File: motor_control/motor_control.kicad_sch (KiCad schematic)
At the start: 24 parts, among them J1 GPIO, J2 MotA, J3 MotB, J4 MOT_POW, J5 UART, J6 SPI, J7 I2C, J8 VBUS_OUT, SW1 PU, SW2 PD, U1 HC-SR04

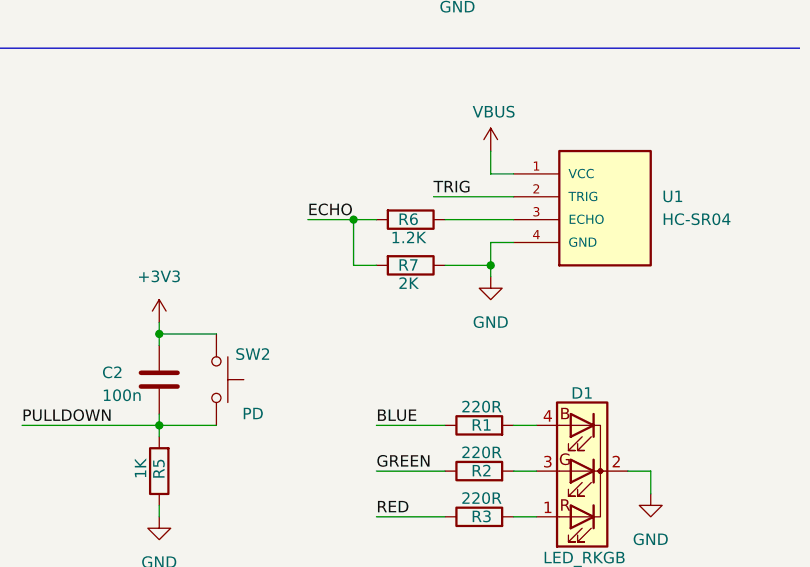
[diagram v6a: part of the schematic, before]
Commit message: fix hcsr04 voltage divider
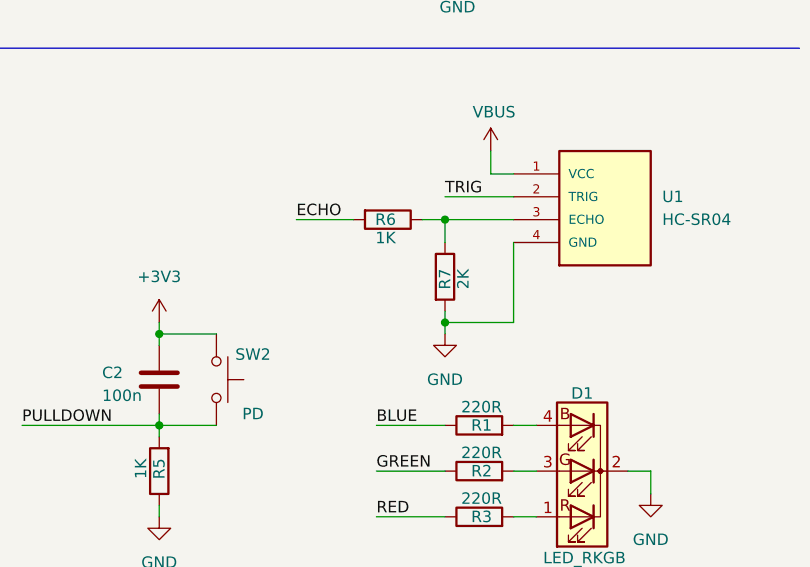
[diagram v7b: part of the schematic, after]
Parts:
- R6: value 1.2K -> 1K
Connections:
- net ECHO: no longer R7.2
- net GND: now also R7.2; no longer R7.1
- net at R6.1, U1.3 (ECHO): now also R7.1
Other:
- moved on the sheet: R6, R7
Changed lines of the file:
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@@
 	)
 	(junction
+		(at 227.33 125.73)
+		(diameter 0)
+		(color 0 0 0 0)
+	)
+	(junction
 		(at 195.58 138.43)
 		(diameter 0)
@@
 	)
 	(junction
-		(at 217.17 125.73)
-		(diameter 0)
-		(color 0 0 0 0)
-	)
-	(junction
 		(at 165.1 158.75)
 		(diameter 0)
@@
 	)
 	(junction
-		(at 232.41 130.81)
-		(diameter 0)
-		(color 0 0 0 0)
-	)
-	(junction
 		(at 165.1 148.59)
 		(diameter 0)
@@
 	)
 	(junction
+		(at 227.33 137.16)
+		(diameter 0)
+		(color 0 0 0 0)
+	)
+	(junction
 		(at 55.88 27.94)
 		(diameter 1.016)
@@
 	(wire
 		(pts
-			(xy 232.41 128.27) (xy 232.41 130.81)
-		)
-		(stroke
-			(width 0)
-			(type default)
-		)
-	)
-	(wire
-		(pts
 			(xy 49.53 166.37) (xy 59.69 166.37)
 		)
@@
 	(wire
 		(pts
+			(xy 227.33 137.16) (xy 227.33 138.43)
+		)
+		(stroke
+			(width 0)
+			(type default)
+		)
+	)
+	(wire
+		(pts
 			(xy 58.42 38.1) (xy 58.42 58.42)
 		)
@@
 	(wire
 		(pts
+			(xy 224.79 125.73) (xy 227.33 125.73)
+		)
+		(stroke
+			(width 0)
+			(type default)
+		)
+	)
+	(wire
+		(pts
 			(xy 185.42 67.31) (xy 205.74 67.31)
 		)
@@
 	(wire
 		(pts
+			(xy 227.33 125.73) (xy 227.33 128.27)
+		)
+		(stroke
+			(width 0)
+			(type default)
+		)
+	)
+	(wire
+		(pts
 			(xy 85.09 168.91) (xy 93.98 168.91)
 		)
@@
 	(wire
 		(pts
-			(xy 232.41 130.81) (xy 232.41 132.08)
-		)
-		(stroke
-			(width 0)
-			(type default)
-		)
-	)
-	(wire
-		(pts
 			(xy 260.35 22.86) (xy 260.35 25.4)
 		)
@@
 	(wire
 		(pts
+			(xy 210.82 125.73) (xy 217.17 125.73)
+		)
+		(stroke
+			(width 0)
+			(type default)
+		)
+	)
+	(wire
+		(pts
 			(xy 251.46 57.15) (xy 264.16 57.15)
 		)
@@
 	(wire
 		(pts
-			(xy 165.1 147.32) (xy 165.1 148.59)
+			(xy 227.33 137.16) (xy 234.95 137.16)
 		)
 		(stroke
@@
 	(wire
 		(pts
-			(xy 40.64 181.61) (xy 59.69 181.61)
+			(xy 165.1 147.32) (xy 165.1 148.59)
 		)
 		(stroke
@@
 	(wire
 		(pts
-			(xy 165.1 148.59) (xy 165.1 149.86)
+			(xy 40.64 181.61) (xy 59.69 181.61)
 		)
 		(stroke
@@
 	(wire
 		(pts
-			(xy 76.2 68.58) (xy 73.66 68.58)
+			(xy 165.1 148.59) (xy 165.1 149.86)
 		)
 		(stroke
 			(width 0)
-			(type solid)
+			(type default)
 		)
 	)
 	(wire
 		(pts
-			(xy 226.06 123.19) (xy 234.95 123.19)
+			(xy 76.2 68.58) (xy 73.66 68.58)
 		)
 		(stroke
 			(width 0)
-			(type default)
+			(type solid)
 		)
 	)
@@
 	(wire
 		(pts
-			(xy 217.17 130.81) (xy 217.17 125.73)
-		)
-		(stroke
-			(width 0)
-			(type default)
-		)
-	)
-	(wire
-		(pts
 			(xy 76.2 43.18) (xy 76.2 50.8)
 		)
@@
 	(wire
 		(pts
-			(xy 234.95 128.27) (xy 232.41 128.27)
-		)
-		(stroke
-			(width 0)
-			(type default)
-		)
-	)
-	(wire
-		(pts
 			(xy 76.2 43.18) (xy 73.66 43.18)
 		)
@@
 	(wire
 		(pts
-			(xy 165.1 158.75) (xy 171.45 158.75)
+			(xy 227.33 135.89) (xy 227.33 137.16)
 		)
 		(stroke
@@
 	(wire
 		(pts
-			(xy 73.66 48.26) (xy 100.33 48.26)
+			(xy 165.1 158.75) (xy 171.45 158.75)
 		)
 		(stroke
 			(width 0)
-			(type solid)
+			(type default)
 		)
 	)
 	(wire
 		(pts
-			(xy 73.66 38.1) (xy 100.33 38.1)
+			(xy 73.66 48.26) (xy 100.33 48.26)
 		)
 		(stroke
@@
 	(wire
 		(pts
-			(xy 227.33 125.73) (xy 234.95 125.73)
+			(xy 73.66 38.1) (xy 100.33 38.1)
 		)
 		(stroke
 			(width 0)
-			(type default)
+			(type solid)
 		)
 	)
@@
 	(wire
 		(pts
-			(xy 227.33 130.81) (xy 232.41 130.81)
-		)
-		(stroke
-			(width 0)
-			(type default)
-		)
-	)
-	(wire
-		(pts
 			(xy 76.2 30.48) (xy 73.66 30.48)
 		)
@@
 	(wire
 		(pts
-			(xy 201.93 138.43) (xy 195.58 138.43)
+			(xy 227.33 123.19) (xy 234.95 123.19)
 		)
 		(stroke
@@
 	(wire
 		(pts
-			(xy 217.17 125.73) (xy 219.71 125.73)
+			(xy 201.93 138.43) (xy 195.58 138.43)
 		)
 		(stroke
@@
 	(wire
 		(pts
+			(xy 227.33 125.73) (xy 234.95 125.73)
+		)
+		(stroke
+			(width 0)
+			(type default)
+		)
+	)
+	(wire
+		(pts
 			(xy 40.64 179.07) (xy 40.64 181.61)
 		)
@@
 	(wire
 		(pts
-			(xy 219.71 130.81) (xy 217.17 130.81)
+			(xy 234.95 128.27) (xy 234.95 137.16)
 		)
 		(stroke
@@
 	(wire
 		(pts
-			(xy 212.09 125.73) (xy 217.17 125.73)
-		)
-		(stroke
-			(width 0)
-			(type default)
-		)
-	)
-	(wire
-		(pts
 			(xy 31.75 129.54) (xy 43.18 129.54)
 		)
@@
 	)
 	(label "ECHO"
-		(at 212.09 125.73 0)
+		(at 210.82 125.73 0)
 		(effects
 			(font
@@
 	)
 	(label "TRIG"
-		(at 226.06 123.19 0)
+		(at 227.33 123.19 0)
 		(effects
 			(font
@@
 	(symbol
 		(lib_id "Device:R")
-		(at 223.52 125.73 270)
+		(at 220.98 125.73 270)
 		(unit 1)
 		(exclude_from_sim no)
@@
 		(dnp no)
 		(property "Reference" "R6"
-			(at 223.266 125.73 90)
+			(at 220.726 125.73 90)
 			(effects
 				(font
@@
 			)
 		)
-		(property "Value" "1.2K"
-			(at 223.266 127.762 90)
+		(property "Value" "1K"
+			(at 220.726 127.762 90)
 			(effects
 				(font
@@
 		)
 		(property "Footprint" "Resistor_THT:R_Axial_DIN0207_L6.3mm_D2.5mm_P7.62mm_Horizontal"
-			(at 223.52 123.952 90)
+			(at 220.98 123.952 90)
 			(effects
 				(font
@@
 		)
 		(property "Datasheet" "~"
-			(at 223.52 125.73 0)
+			(at 220.98 125.73 0)
 			(effects
 				(font
@@
 		)
 		(property "Description" "Resistor"
-			(at 223.52 125.73 0)
+			(at 220.98 125.73 0)
 			(effects
 				(font
@@
 	(symbol
 		(lib_id "Device:R")
-		(at 223.52 130.81 270)
+		(at 227.33 132.08 0)
 		(unit 1)
 		(exclude_from_sim no)
@@
 		(dnp no)
 		(property "Reference" "R7"
-			(at 223.266 130.81 90)
+			(at 227.33 132.334 90)
 			(effects
 				(font
@@
 		)
 		(property "Value" "2K"
-			(at 223.266 132.842 90)
+			(at 229.362 132.334 90)
 			(effects
 				(font
@@
 		)
 		(property "Footprint" "Resistor_THT:R_Axial_DIN0207_L6.3mm_D2.5mm_P7.62mm_Horizontal"
-			(at 223.52 129.032 90)
+			(at 225.552 132.08 90)
 			(effects
 				(font
@@
 		)
 		(property "Datasheet" "~"
-			(at 223.52 130.81 0)
+			(at 227.33 132.08 0)
 			(effects
 				(font
@@
 		)
 		(property "Description" "Resistor"
-			(at 223.52 130.81 0)
+			(at 227.33 132.08 0)
 			(effects
 				(font
@@
 	(symbol
 		(lib_id "power:GND")
-		(at 232.41 132.08 0)
+		(at 227.33 138.43 0)
 		(unit 1)
 		(exclude_from_sim no)
@@
 		(fields_autoplaced yes)
 		(property "Reference" "#PWR012"
-			(at 232.41 138.43 0)
+			(at 227.33 144.78 0)
 			(effects
 				(font
@@
 		)
 		(property "Value" "GND"
-			(at 232.41 137.16 0)
+			(at 227.33 143.51 0)
 			(effects
 				(font
@@
 		)
 		(property "Footprint" ""
-			(at 232.41 132.08 0)
+			(at 227.33 138.43 0)
 			(effects
 				(font
@@
 		)
 		(property "Datasheet" ""
-			(at 232.41 132.08 0)
+			(at 227.33 138.43 0)
 			(effects
 				(font
@@
 		)
 		(property "Description" "Power symbol creates a global label with name \"GND\" , ground"
-			(at 232.41 132.08 0)
+			(at 227.33 138.43 0)
 			(effects
 				(font

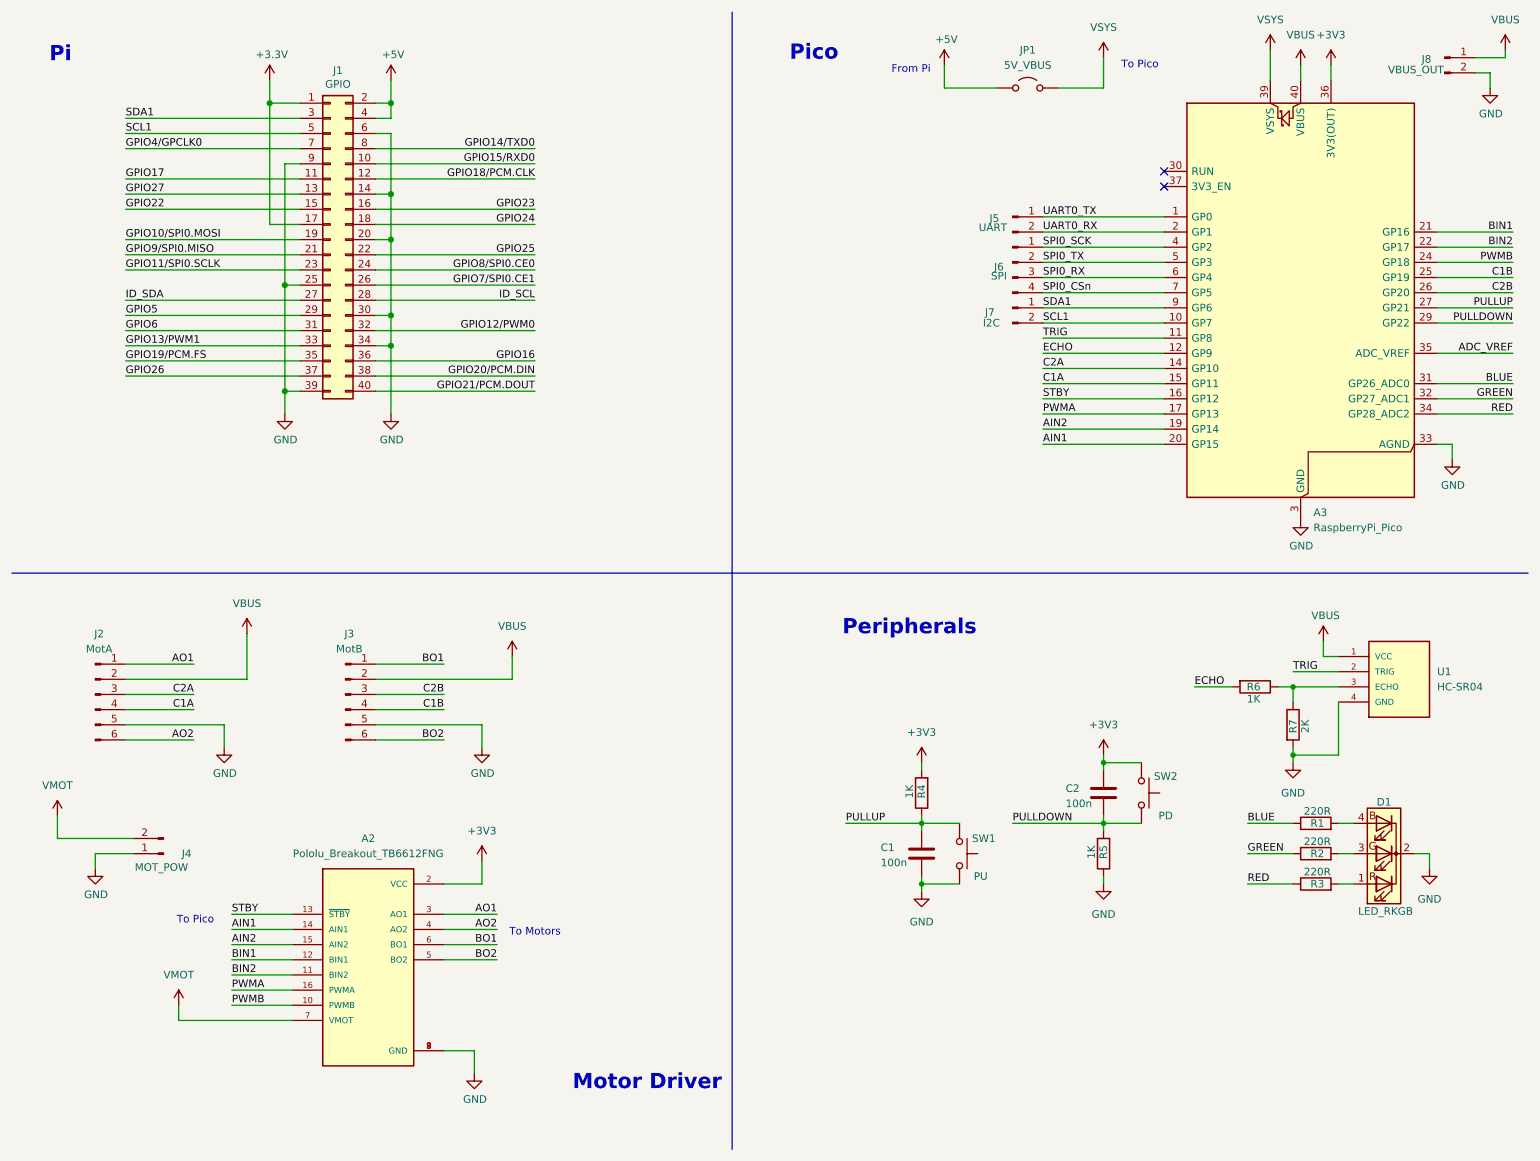
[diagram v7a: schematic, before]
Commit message: update schematic and pcb
1. added a input 01x02 header for PEB power up +5V
2. switched to +5V to power up sonar and encoders
3. set jumper between +5V and PEB 5V input
4. upgraded motor driver input to JST-XH
5. updated footprints
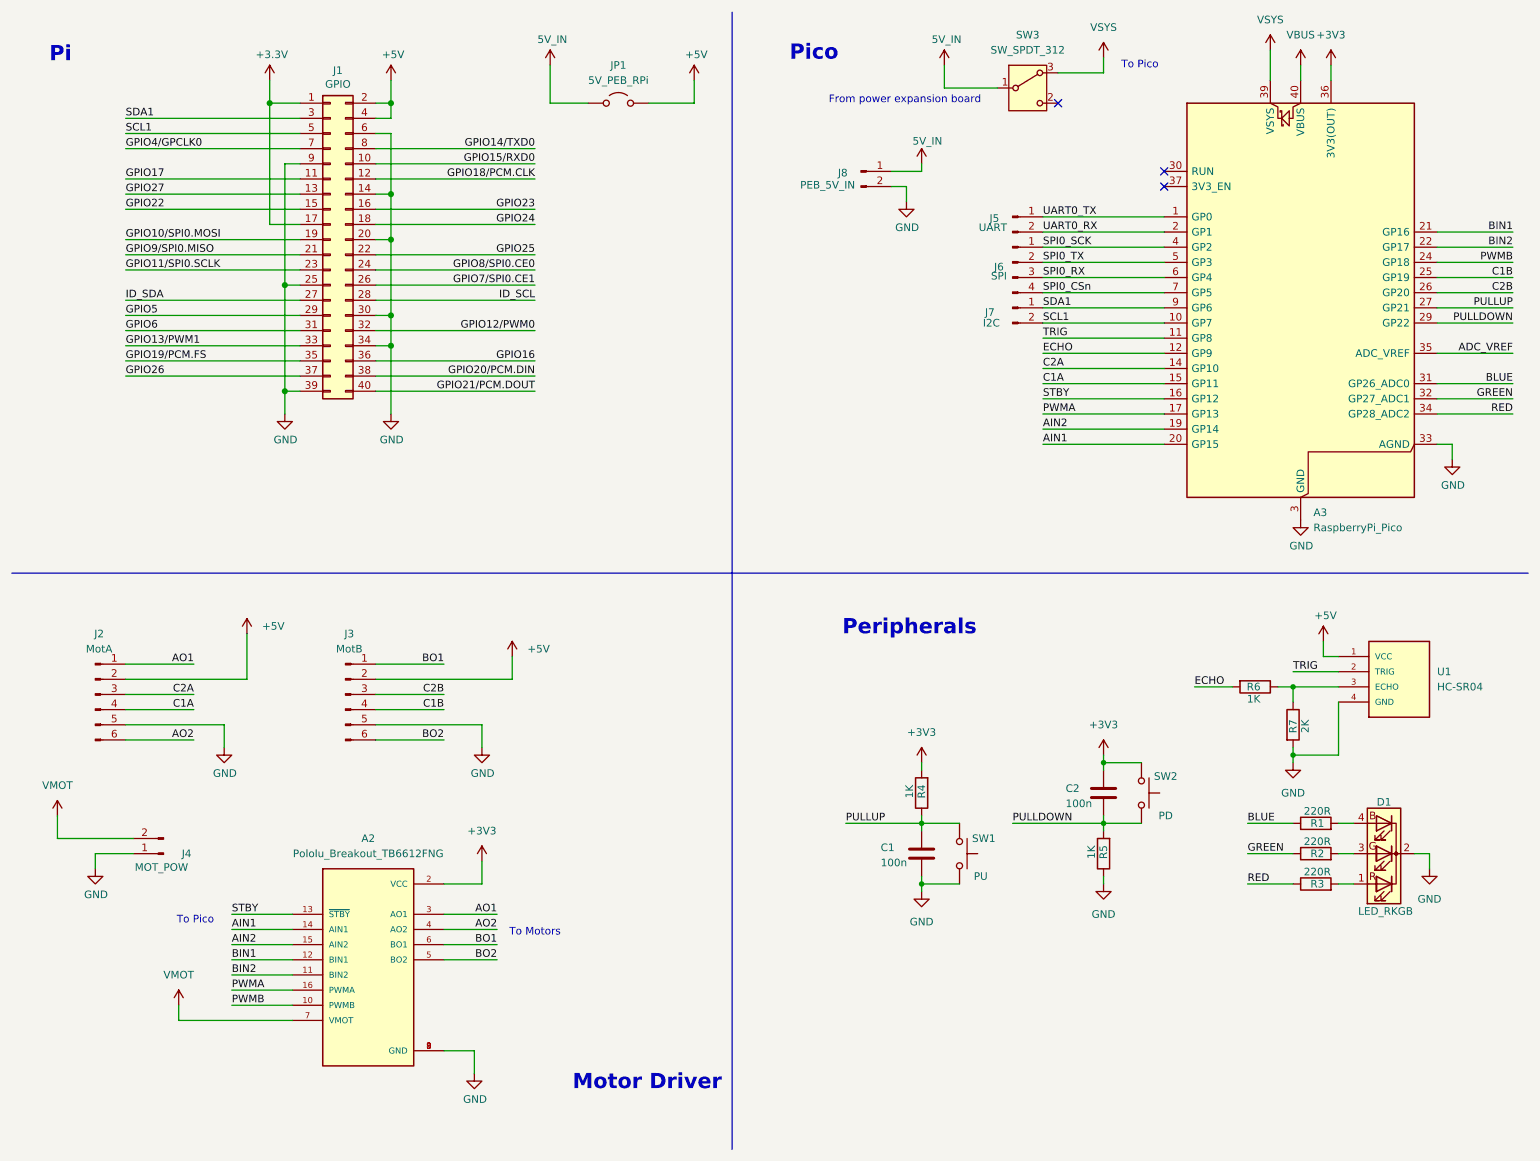
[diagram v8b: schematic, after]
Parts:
- added SW3: SW_SPDT_312, Button_Switch_THT:SW_Slide-03_Wuerth-WS-SLTV_10x2.5x6.4_P2.54mm, symbol Switch:SW_SPDT_312
- J4: footprint Connector_PinHeader_2.54mm:PinHeader_1x02_P2.54mm_Horizontal -> Connector_JST:JST_XH_S2B-XH-A_1x02_P2.50mm_Horizontal
- J8: value VBUS_OUT -> PEB_5V_IN
- JP1: value 5V_VBUS -> 5V_PEB_RPi
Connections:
- net +5V: now also J2.2 (Pin_2), J3.2 (Pin_2), JP1.2 (B), U1.1 (VCC); no longer JP1.1 (A)
- net VBUS: no longer J2.2 (Pin_2), J3.2 (Pin_2), J8.1 (Pin_1), U1.1 (VCC)
- net VSYS: now also SW3.3 (A); no longer JP1.2 (B)
- new net 5V_IN: J8.1 (Pin_1), JP1.1 (A), SW3.1 (B)
- no-connect marks 2 -> 3
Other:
- note added: "From power expansion board"
- note removed: "From Pi"
- moved on the sheet: J8, JP1
